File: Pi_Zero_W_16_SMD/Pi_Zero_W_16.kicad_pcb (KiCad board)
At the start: 2 copper layers, 142.1 x 93 mm, 102 parts, among them J1 String1, J10 String10, J11 String11, J12 String12, J13 String13, J14 String14, J15 String15, J16 String16, J17 Power In Left, J18 Power In Right, J19 Aux Pwr, J2 String2, J20 VIN Select, J21 VIN Voltage, J22 OLED Conn, J23 Diff Out, J24 Diff Out, J3 String3, J4 String4, J5 String5, J6 String6, J7 String7, J8 String8, J9 String9, Q1 DMP3056L, SW1 Enter BTN, SW2 Down BTN, U1 Raspberry Pi Zero W, U2 SN74HCT245N, U3 SN74HCT245N, U4 AM26C31, U5 AM26C31, U6 24LC256, U7 Universe5V

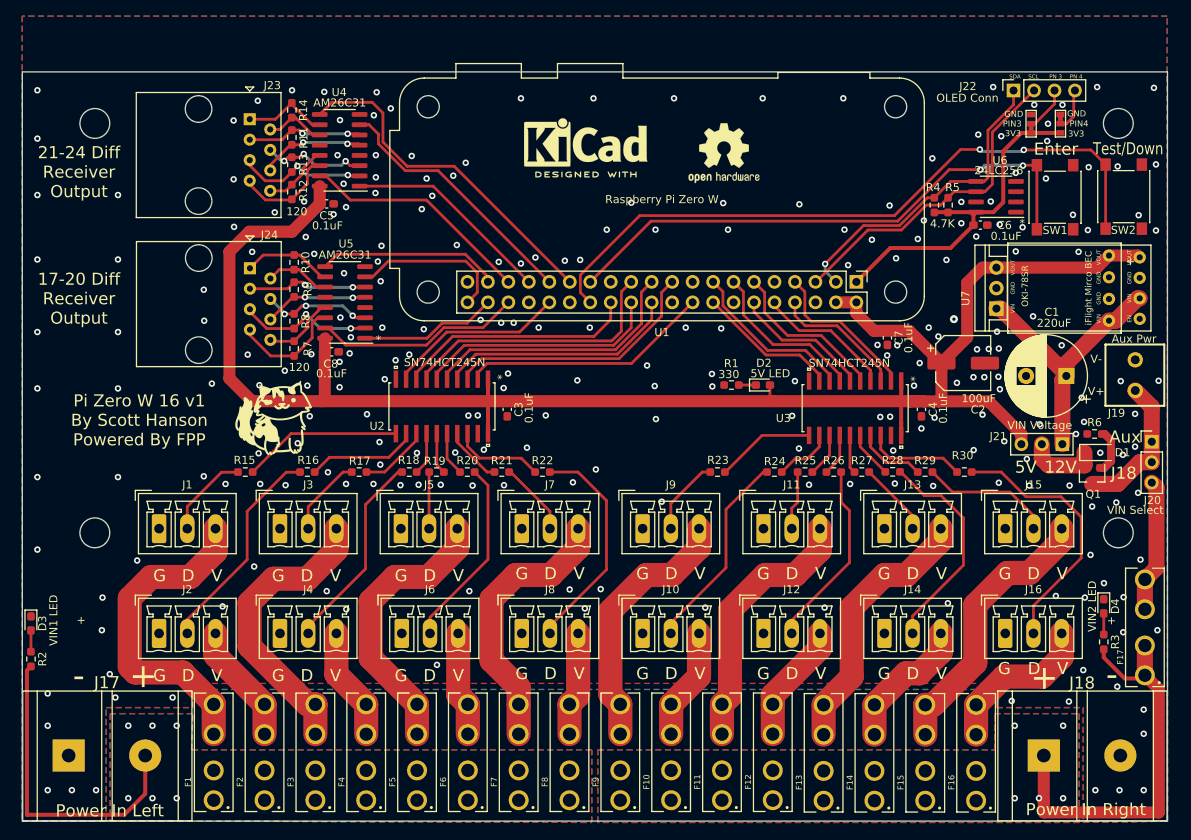
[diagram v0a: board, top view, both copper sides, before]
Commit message: switched to 3.81mm connectors
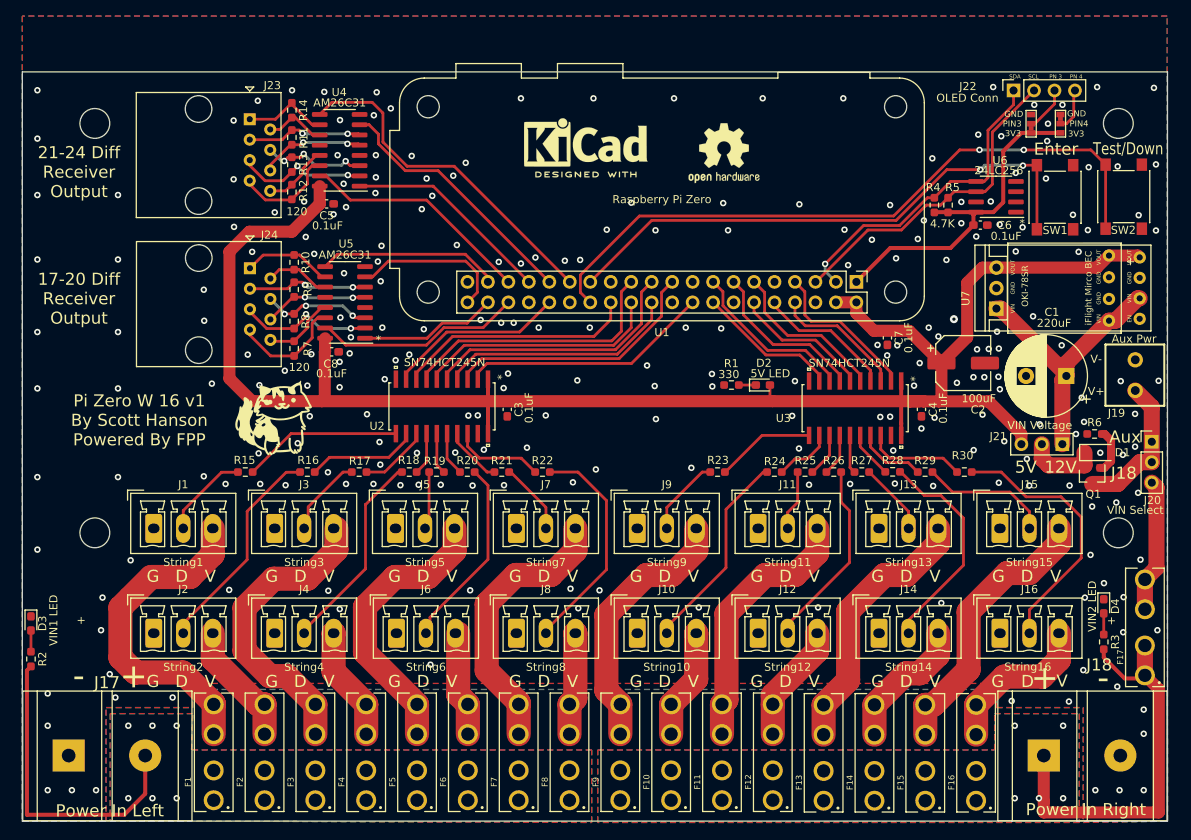
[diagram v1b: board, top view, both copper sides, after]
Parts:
- J1, J10, J11, J12, J13, J14, J15, J16, J2, J3, J4, J5, J6, J7, J8, J9: footprint Connector_Phoenix_MC:PhoenixContact_MCV_1,5_3-G-3.5_1x03_P3.50mm_Vertical -> Scotts:PhoenixContact_MCV_3.81mm_3.5mm_1x03_Vertical
- U1: value Raspberry Pi Zero W -> Raspberry Pi Zero
- moved J1 0.81 mm to (88.3, 116.6)
- moved J2 0.81 mm to (88.3, 129.6)
- moved J3 0.81 mm to (103.3, 116.6)
- moved J4 0.81 mm to (103.3, 129.6)
- moved J5 0.81 mm to (118.3, 116.6)
- moved J6 0.81 mm to (118.4, 129.6)
- moved J10 0.81 mm to (148.3, 129.6)
- moved J11 0.81 mm to (163.3, 116.6)
- moved J12 0.81 mm to (163.3, 129.6)
- moved J13 0.81 mm to (178.3, 116.6)
- moved J14 0.81 mm to (178.3, 129.6)
- moved J15 0.81 mm to (193.3, 116.6)
- moved J16 0.81 mm to (193.3, 129.6)
- moved J7 0.81 mm to (133.3, 116.6)
- moved J8 0.81 mm to (133.3, 129.6)
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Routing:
- net /Output 9-16/DOUT12: track 25.0 -> 23.6 mm
- net /Output 1-8/DOUT1: track 12.4 -> 11.0 mm
- net /Output 1-8/VOUT3: track 36.5 -> 37.6 mm
- net /Output 1-8/VOUT1: track 40.5 -> 41.3 mm
- net /Output 1-8/VOUT2: track 15.0 -> 15.7 mm
- net GND: vias 250 -> 248

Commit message: fixes
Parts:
- SW1, SW2: footprint Button_Switch_SMD:SW_Push_1P1T_NO_6x6mm_H9.5mm -> Scotts:SW_Push_1P1T_NO_6x6mm_H9.5mm
- moved D1 0.23 mm to (205.6, 106.9)
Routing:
- net OUT23+: track 16.4 -> 17.0 mm
- net OUT23-: track 13.0 -> 13.6 mm
- net GND: vias 248 -> 250
